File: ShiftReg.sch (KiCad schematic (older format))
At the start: 1 part, among them U21 MCP23S17_SO

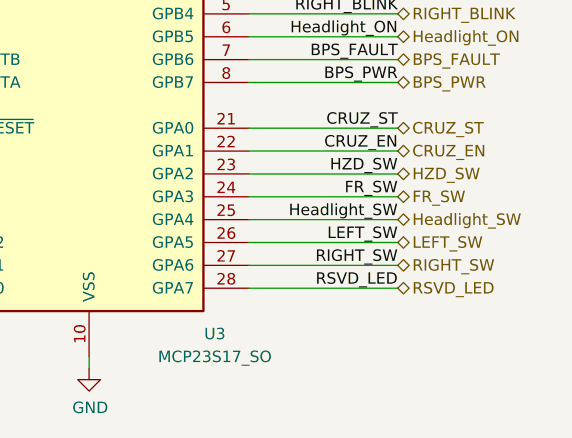
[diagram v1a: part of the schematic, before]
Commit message: Added Regen switch, deleted RSVD LED
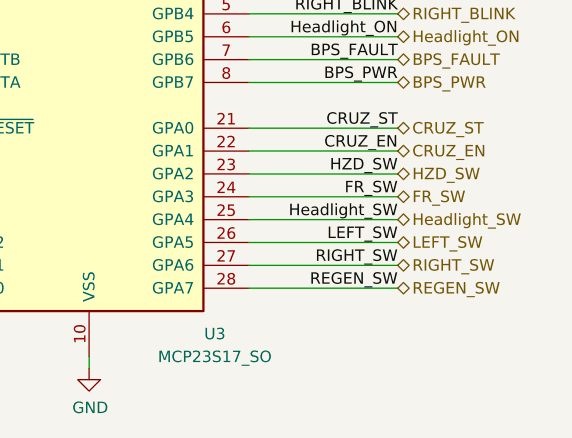
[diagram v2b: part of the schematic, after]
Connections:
- net RSVD_LED renamed REGEN_SW
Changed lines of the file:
@@
 M_CNCTR
 Text HLabel 7200 4900 2    50   BiDi ~ 0
-RSVD_LED
+REGEN_SW
 Text HLabel 7200 3500 2    50   BiDi ~ 0
 CTRL_FAULT
@@
 RIGHT_SW
 Text Label 7200 4900 2    50   ~ 0
-RSVD_LED
+REGEN_SW
 Wire Wire Line
 	6550 4900 7200 4900

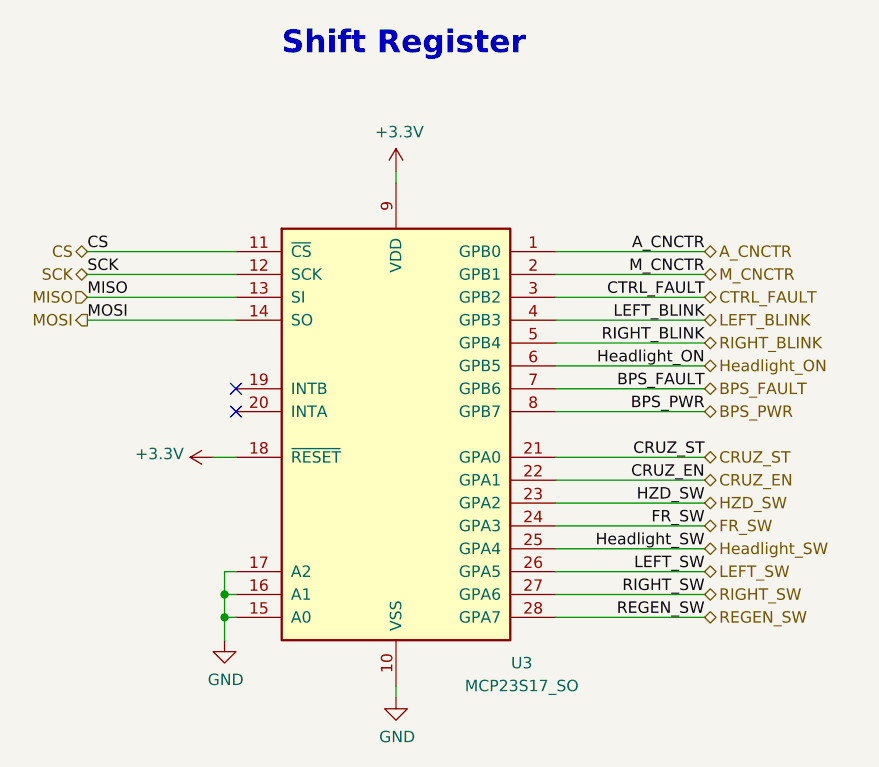
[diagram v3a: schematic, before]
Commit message: Updated schematic with changed F/W switch and BPS_PWR direct connection to MinionConn
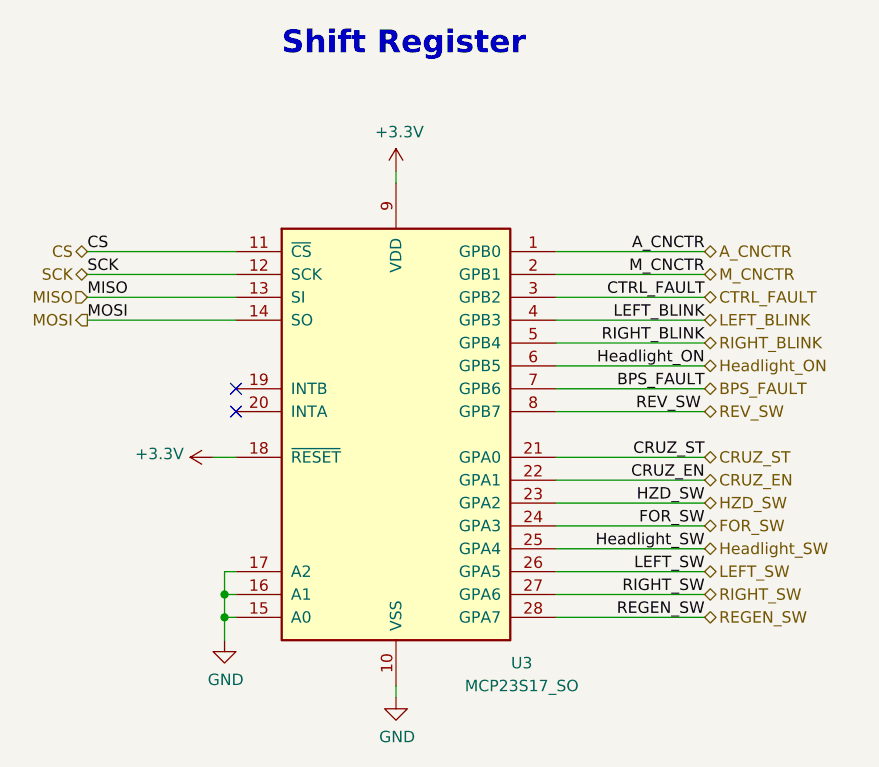
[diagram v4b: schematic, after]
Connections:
- net BPS_PWR renamed REV_SW
- net FR_SW renamed FOR_SW
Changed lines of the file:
@@
 Headlight_SW
 Text Label 7200 4500 2    50   ~ 0
-FR_SW
+FOR_SW
 Text Label 7200 4400 2    50   ~ 0
 HZD_SW
@@
 Wire Wire Line
 	6550 4000 7200 4000
-Text Label 7200 4000 2    50   ~ 0
-BPS_PWR
 Text Label 7200 3600 2    50   ~ 0
 LEFT_BLINK
@@
 Text HLabel 7200 3600 2    50   BiDi ~ 0
 LEFT_BLINK
-Text HLabel 7200 4000 2    50   BiDi ~ 0
-BPS_PWR
 Text HLabel 7200 4200 2    50   BiDi ~ 0
 CRUZ_ST
@@
 HZD_SW
 Text HLabel 7200 4500 2    50   BiDi ~ 0
-FR_SW
+FOR_SW
 Text HLabel 7200 4600 2    50   BiDi ~ 0
 Headlight_SW
@@
 Text HLabel 7200 4900 2    50   BiDi ~ 0
 REGEN_SW
+Text Label 6900 4000 0    50   ~ 0
+REV_SW
+Text HLabel 7200 4000 2    50   BiDi ~ 0
+REV_SW
 $EndSCHEMATC

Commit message: Finished current updates to the board
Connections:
- net HZD_SW: now also U21.8 (GPB7); no longer U21.23 (GPA2)
- net REV_SW: now also U21.23 (GPA2); no longer U21.8 (GPB7)
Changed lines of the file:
@@
 Text Label 7200 4500 2    50   ~ 0
 FOR_SW
-Text Label 7200 4400 2    50   ~ 0
+Text Label 7200 4000 2    50   ~ 0
 HZD_SW
 Text Label 7200 4300 2    50   ~ 0
@@
 Text HLabel 7200 4300 2    50   BiDi ~ 0
 CRUZ_EN
-Text HLabel 7200 4400 2    50   BiDi ~ 0
+Text HLabel 7200 4000 2    50   BiDi ~ 0
 HZD_SW
 Text HLabel 7200 4500 2    50   BiDi ~ 0
@@
 Text HLabel 7200 4900 2    50   BiDi ~ 0
 REGEN_SW
-Text Label 6900 4000 0    50   ~ 0
+Text Label 6900 4400 0    50   ~ 0
 REV_SW
-Text HLabel 7200 4000 2    50   BiDi ~ 0
+Text HLabel 7200 4400 2    50   BiDi ~ 0
 REV_SW
 $EndSCHEMATC
